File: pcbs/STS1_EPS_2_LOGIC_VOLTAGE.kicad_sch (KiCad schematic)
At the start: 7 parts, among them U11 LTC4451AV#TRMPBF, U12 LTC4451AV#TRMPBF

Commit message: Separated the SHDN pins of the logic- and power oring. Also added TVS diodes to them, as this is recommended by the datasheet.
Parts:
- added D6: SMF5.0A, Diode_SMD:D_SMF, symbol Device:D_Zener
- added D7: SMF8.0A-HF, Diode_SMD:D_SOD-123F, symbol Device:D_Zener
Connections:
- net BATT_RAW: now also D7.1 (K); no longer U12.16 (~{SHDN})
- net GND: now also D6.2 (A), D7.2 (A)
- net MPPT_BUS: now also U12.16 (~{SHDN}), D6.1 (K)

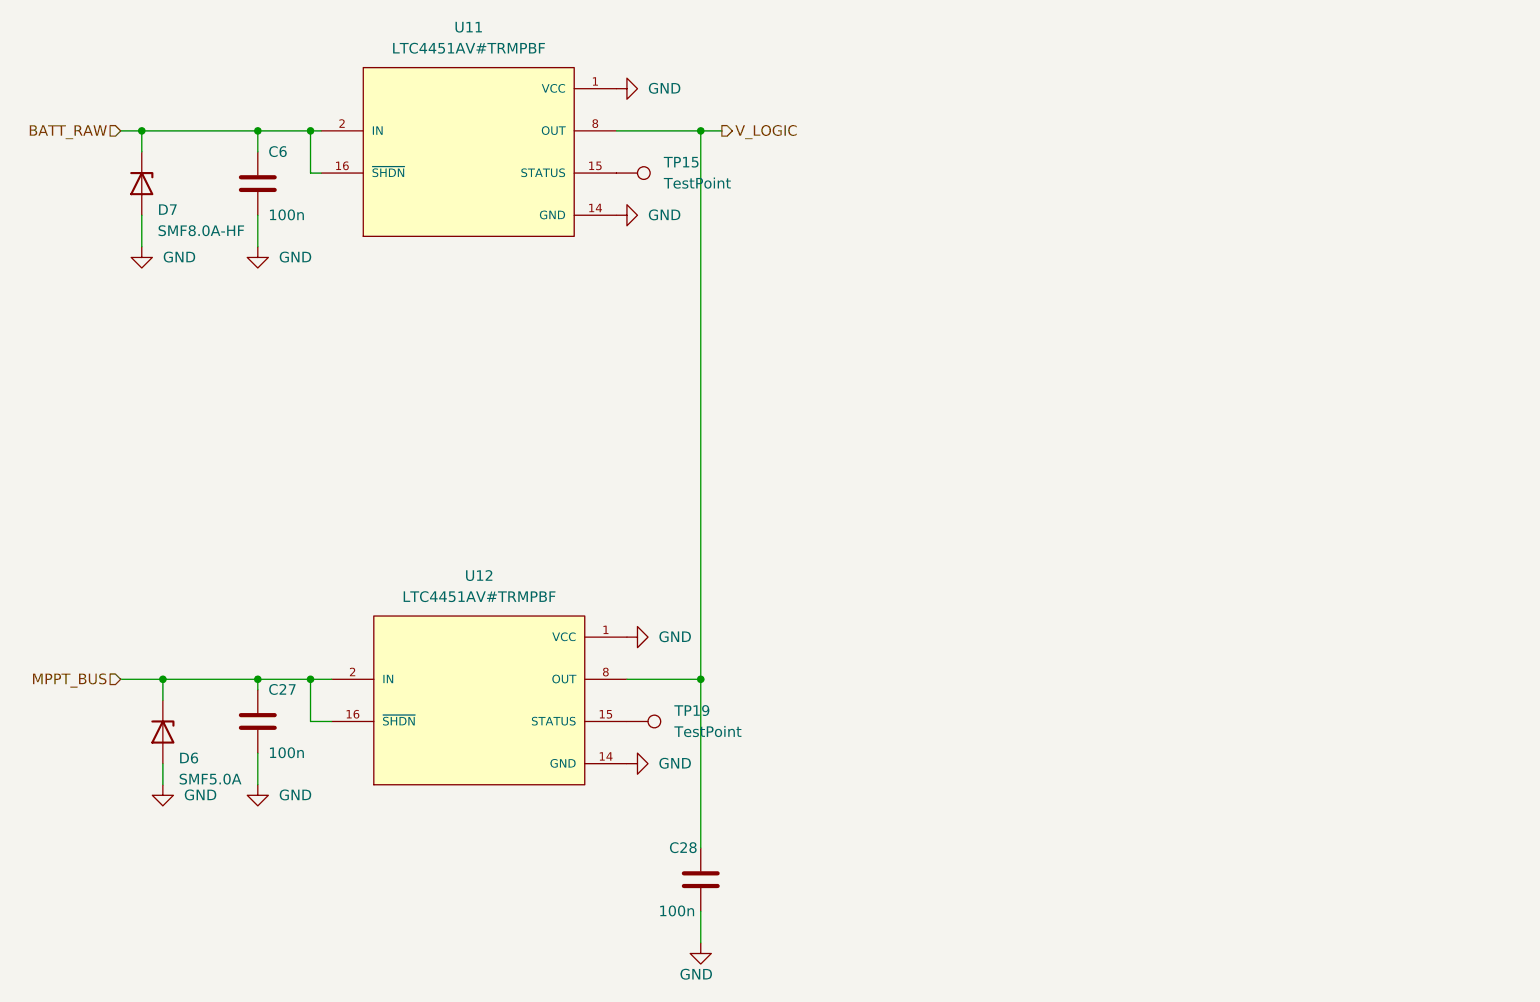
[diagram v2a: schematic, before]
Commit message: Added a linear regulator to the power oring in STS1_EPS_2, since the components supplied by that power oring could not withstand that voltage.
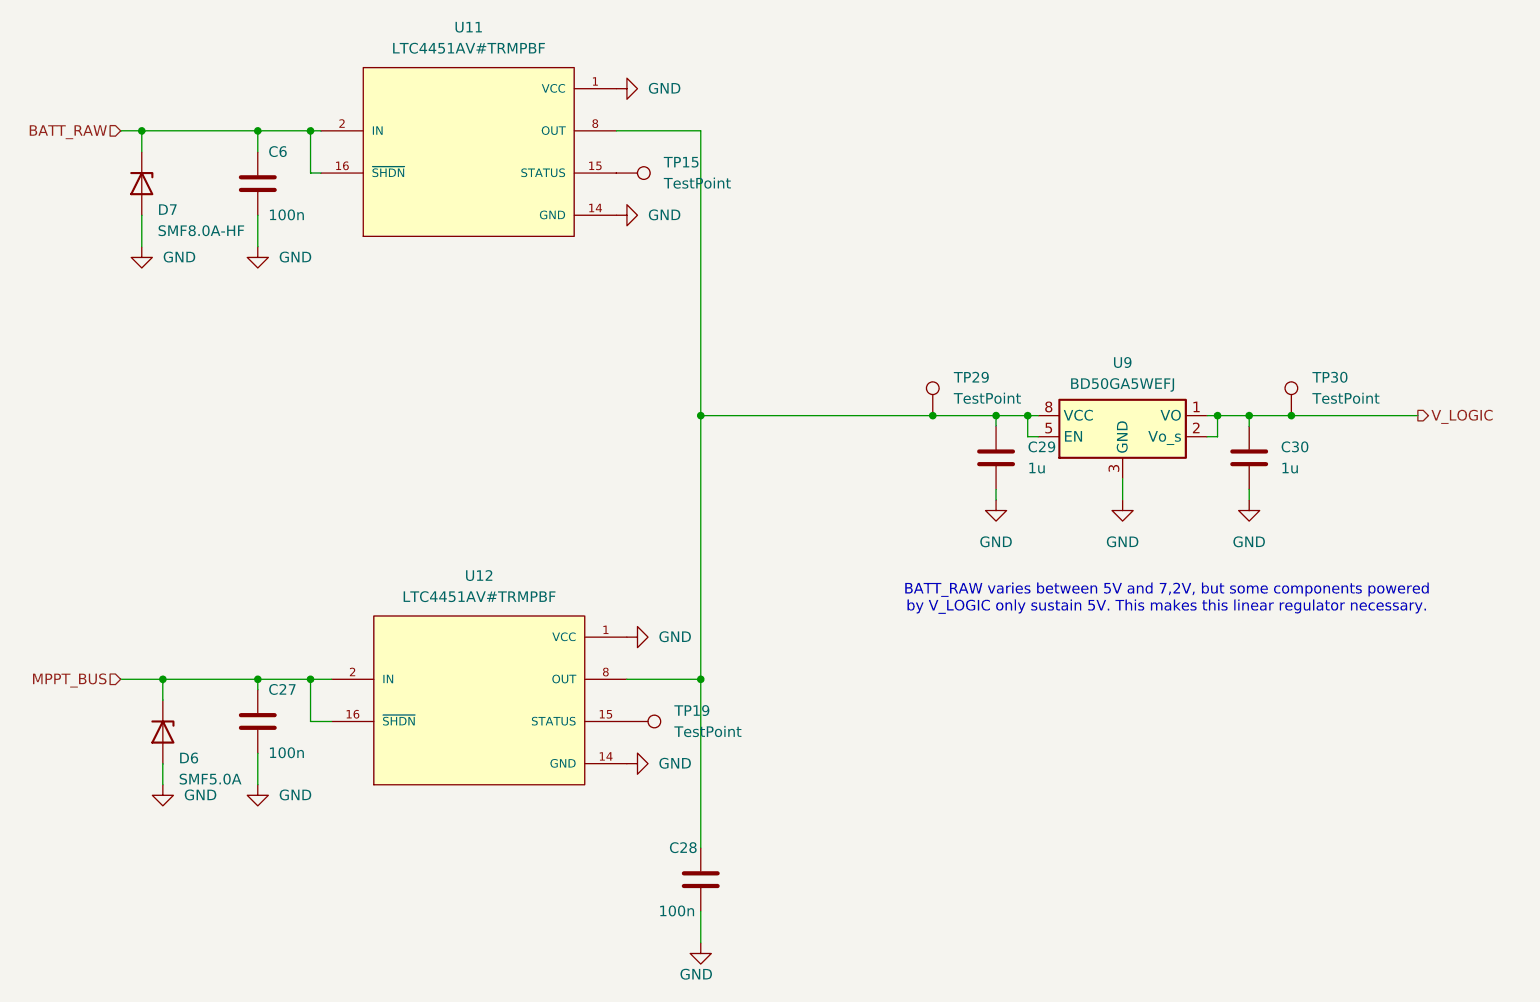
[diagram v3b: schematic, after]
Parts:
- added C29, C30: 1u, Capacitor_SMD:C_0805_2012Metric, symbol Device:C
- added TP29, TP30: TestPoint, TestPoint:TestPoint_THTPad_D1.0mm_Drill0.5mm, symbol Connector:TestPoint
- added U9: BD50GA5WEFJ, Package_SO:HTSOP-8-1EP_3.9x4.9mm_P1.27mm_EP2.4x3.2mm, symbol Regulator_Linear:BD50GA5WEFJ
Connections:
- net GND: now also C29.2, C30.2, U9.3 (GND), U9.4 (GND), U9.6 (GND), U9.7 (GND), U9.9 (GND)
- net V_LOGIC: now also C30.1, TP30.1, U9.1 (VO), U9.2 (Vo_s); no longer C28.1, U11.8 (OUT), U12.8 (OUT)
- new net: C28.1, C29.1, TP29.1, U11.8 (OUT), U12.8 (OUT), U9.5 (EN), U9.8 (VCC)
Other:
- note added: "BATT_RAW varies between 5V and 7,2V, but some components powered by V_LOGIC only sustain 5V. This makes this linear regulator necessary."
